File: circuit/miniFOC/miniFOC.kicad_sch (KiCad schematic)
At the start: 68 parts, among them J1 Conn_01x05, J2 Conn_01x06, J3 Conn_01x02, J4 Conn_01x01, J5 Conn_01x01, J6 Conn_01x01, Q1 AP30H50Q, Q2 AP30H50Q, Q3 AP30H50Q, Q4 AP30H50Q, Q5 AP30H50Q, Q6 AP30H50Q, U1 XC6206P332MR, U2 AT32F421C8, U3 LM321, U4 COS722MR, U5 EG2133, U6 JW5017S

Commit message: Completed PCB drawing of miniFOC sensor board
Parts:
- C26: footprint Capacitor_SMD:C_0603_1608Metric_Pad1.08x0.95mm_HandSolder -> Capacitor_SMD:C_0402_1005Metric
- C27, C28, C29: footprint Capacitor_SMD:C_0603_1608Metric_Pad1.08x0.95mm_HandSolder -> Capacitor_SMD:C_0603_1608Metric
- C3, C6: footprint Capacitor_SMD:C_1206_3216Metric_Pad1.33x1.80mm_HandSolder -> Capacitor_SMD:C_0603_1608Metric
- J2: footprint (none) -> Connector_JST:JST_GH_SM06B-GHS-TB_1x06-1MP_P1.25mm_Horizontal
- J3: footprint (none) -> Connector_Wire:SolderWire-0.1sqmm_1x02_P3.6mm_D0.4mm_OD1mm
- J4, J5, J6: footprint (none) -> Connector_PinHeader_2.54mm:PinHeader_1x01_P2.54mm_Vertical
- L1: footprint PowerLibrary:IND-SMD_L4.6-W4.2_SMMS0420 -> Inductor_SMD:L_Coilcraft_XxL4040
- R13, R15, R16: footprint Resistor_SMD:R_0603_1608Metric_Pad0.98x0.95mm_HandSolder -> Capacitor_SMD:C_0402_1005Metric
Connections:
- net TIM1_CH1: now also U5.3 (HIN3), U5.6 (~{LIN3}); no longer U5.1 (HIN1), U5.4 (~{LIN1})
- net TIM1_CH3: now also U5.1 (HIN1), U5.4 (~{LIN1}); no longer U5.3 (HIN3), U5.6 (~{LIN3})
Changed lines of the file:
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@@
   (title_block
     (title "miniFOC")
-    (date "2022-10-11")
+    (date "2022-10-21")
     (rev "1.2.1")
   )
@@
     (effects (font (size 1.27 1.27)) (justify right bottom))
   )
-  (label "TIM1_CH1" (at 153.67 55.88 0)
+  (label "TIM1_CH1" (at 153.67 60.96 0)
     (effects (font (size 1.27 1.27)) (justify left bottom))
   )
@@
     (effects (font (size 1.27 1.27)) (justify left bottom))
   )
-  (label "TIM1_CH3" (at 153.67 60.96 0)
+  (label "TIM1_CH3" (at 153.67 55.88 0)
     (effects (font (size 1.27 1.27)) (justify left bottom))
   )
@@
       (effects (font (size 1.27 1.27)) (justify left) hide)
     )
-    (property "Footprint" "" (id 2) (at 274.32 76.2 0)
+    (property "Footprint" "Connector_PinHeader_2.54mm:PinHeader_1x01_P2.54mm_Vertical" (id 2) (at 274.32 76.2 0)
       (effects (font (size 1.27 1.27)) hide)
     )
@@
       (effects (font (size 1.27 1.27)) (justify right) hide)
     )
-    (property "Footprint" "Capacitor_SMD:C_0603_1608Metric_Pad1.08x0.95mm_HandSolder" (id 2) (at 267.0048 151.13 0)
+    (property "Footprint" "Capacitor_SMD:C_0603_1608Metric" (id 2) (at 267.0048 151.13 0)
       (effects (font (size 1.27 1.27)) hide)
     )
@@
       (effects (font (size 1.27 1.27)) (justify right))
     )
-    (property "Footprint" "Capacitor_SMD:C_1206_3216Metric_Pad1.33x1.80mm_HandSolder" (id 2) (at 49.8348 177.8 0)
+    (property "Footprint" "Capacitor_SMD:C_0603_1608Metric" (id 2) (at 49.8348 177.8 0)
       (effects (font (size 1.27 1.27)) hide)
     )
@@
       (effects (font (size 1.27 1.27)) (justify right))
     )
-    (property "Footprint" "Capacitor_SMD:C_1206_3216Metric_Pad1.33x1.80mm_HandSolder" (id 2) (at 19.3548 177.8 0)
+    (property "Footprint" "Capacitor_SMD:C_0603_1608Metric" (id 2) (at 19.3548 177.8 0)
       (effects (font (size 1.27 1.27)) hide)
     )
@@
       (effects (font (size 1.27 1.27)) (justify right))
     )
-    (property "Footprint" "Capacitor_SMD:C_0603_1608Metric_Pad1.08x0.95mm_HandSolder" (id 2) (at 243.84 152.0952 0)
+    (property "Footprint" "Capacitor_SMD:C_0402_1005Metric" (id 2) (at 243.84 152.0952 0)
       (effects (font (size 1.27 1.27)) hide)
     )
@@
       (effects (font (size 1.27 1.27)) (justify right))
     )
-    (property "Footprint" "Resistor_SMD:R_0603_1608Metric_Pad0.98x0.95mm_HandSolder" (id 2) (at 222.758 143.51 90)
+    (property "Footprint" "Capacitor_SMD:C_0402_1005Metric" (id 2) (at 222.758 143.51 90)
       (effects (font (size 1.27 1.27)) hide)
     )
@@
       (effects (font (size 1.27 1.27)) (justify right) hide)
     )
-    (property "Footprint" "Capacitor_SMD:C_0603_1608Metric_Pad1.08x0.95mm_HandSolder" (id 2) (at 261.9248 163.83 0)
+    (property "Footprint" "Capacitor_SMD:C_0603_1608Metric" (id 2) (at 261.9248 163.83 0)
       (effects (font (size 1.27 1.27)) hide)
     )
@@
       (effects (font (size 1.27 1.27)) hide)
     )
-    (property "Footprint" "" (id 2) (at 180.34 157.48 0)
+    (property "Footprint" "Connector_Wire:SolderWire-0.1sqmm_1x02_P3.6mm_D0.4mm_OD1mm" (id 2) (at 180.34 157.48 0)
       (effects (font (size 1.27 1.27)) hide)
     )
@@
       (effects (font (size 1.27 1.27)) (justify left) hide)
     )
-    (property "Footprint" "" (id 2) (at 274.32 60.96 0)
+    (property "Footprint" "Connector_PinHeader_2.54mm:PinHeader_1x01_P2.54mm_Vertical" (id 2) (at 274.32 60.96 0)
       (effects (font (size 1.27 1.27)) hide)
     )
@@
       (effects (font (size 1.27 1.27)) (justify left) hide)
     )
-    (property "Footprint" "" (id 2) (at 134.62 40.64 0)
+    (property "Footprint" "Connector_JST:JST_GH_SM06B-GHS-TB_1x06-1MP_P1.25mm_Horizontal" (id 2) (at 134.62 40.64 0)
       (effects (font (size 1.27 1.27)) hide)
     )
@@
       (effects (font (size 1.27 1.27)) (justify left) hide)
     )
-    (property "Footprint" "" (id 2) (at 274.32 68.58 0)
+    (property "Footprint" "Connector_PinHeader_2.54mm:PinHeader_1x01_P2.54mm_Vertical" (id 2) (at 274.32 68.58 0)
       (effects (font (size 1.27 1.27)) hide)
     )
@@
       (effects (font (size 1.27 1.27)) (justify right))
     )
-    (property "Footprint" "Capacitor_SMD:C_0603_1608Metric_Pad1.08x0.95mm_HandSolder" (id 2) (at 273.3548 151.13 0)
+    (property "Footprint" "Capacitor_SMD:C_0603_1608Metric" (id 2) (at 273.3548 151.13 0)
       (effects (font (size 1.27 1.27)) hide)
     )
@@
       (effects (font (size 1.27 1.27)) (justify right))
     )
-    (property "Footprint" "Resistor_SMD:R_0603_1608Metric_Pad0.98x0.95mm_HandSolder" (id 2) (at 245.618 168.91 90)
+    (property "Footprint" "Capacitor_SMD:C_0402_1005Metric" (id 2) (at 245.618 168.91 90)
       (effects (font (size 1.27 1.27)) hide)
     )
@@
     (property "Reference" "L1" (id 0) (at 257.81 148.59 90))
     (property "Value" "4.7uH" (id 1) (at 257.81 151.13 90))
-    (property "Footprint" "PowerLibrary:IND-SMD_L4.6-W4.2_SMMS0420" (id 2) (at 257.81 153.67 0)
+    (property "Footprint" "Inductor_SMD:L_Coilcraft_XxL4040" (id 2) (at 257.81 153.67 0)
       (effects (font (size 1.27 1.27)) hide)
     )
@@
     (property "Reference" "R16" (id 0) (at 253.365 162.56 90))
     (property "Value" "16kR" (id 1) (at 253.365 164.465 90))
-    (property "Footprint" "Resistor_SMD:R_0603_1608Metric_Pad0.98x0.95mm_HandSolder" (id 2) (at 253.365 158.242 90)
+    (property "Footprint" "Capacitor_SMD:C_0402_1005Metric" (id 2) (at 253.365 158.242 90)
       (effects (font (size 1.27 1.27)) hide)
     )
@@
     )
     (path "/57180d6e-6a91-467d-a82b-02bb6d697214"
-      (reference "C3") (unit 1) (value "10uF") (footprint "Capacitor_SMD:C_1206_3216Metric_Pad1.33x1.80mm_HandSolder")
+      (reference "C3") (unit 1) (value "10uF") (footprint "Capacitor_SMD:C_0603_1608Metric")
     )
     (path "/ebd293f8-a987-417b-a4c4-abe8a2adfd97"
@@
     )
     (path "/1af18610-1415-484c-99c1-d2085ea98a87"
-      (reference "C6") (unit 1) (value "10uF") (footprint "Capacitor_SMD:C_1206_3216Metric_Pad1.33x1.80mm_HandSolder")
+      (reference "C6") (unit 1) (value "10uF") (footprint "Capacitor_SMD:C_0603_1608Metric")
     )
     (path "/5de879fb-dac5-44c4-8df6-5853ed3f2d44"
@@
     )
     (path "/6d0a8729-3a54-430f-8b0f-be4deb3d1c1a"
-      (reference "C26") (unit 1) (value "100nF") (footprint "Capacitor_SMD:C_0603_1608Metric_Pad1.08x0.95mm_HandSolder")
+      (reference "C26") (unit 1) (value "100nF") (footprint "Capacitor_SMD:C_0402_1005Metric")
     )
     (path "/8836bf46-cefc-4f20-9228-b7aa312d1021"
-      (reference "C27") (unit 1) (value "22uF") (footprint "Capacitor_SMD:C_0603_1608Metric_Pad1.08x0.95mm_HandSolder")
+      (reference "C27") (unit 1) (value "22uF") (footprint "Capacitor_SMD:C_0603_1608Metric")
     )
     (path "/15e769c6-5c6f-4f78-96ac-500286d22897"
-      (reference "C28") (unit 1) (value "22uF") (footprint "Capacitor_SMD:C_0603_1608Metric_Pad1.08x0.95mm_HandSolder")
+      (reference "C28") (unit 1) (value "22uF") (footprint "Capacitor_SMD:C_0603_1608Metric")
     )
     (path "/cc13aa9b-0a71-47d7-a701-77ff3ce296df"
-      (reference "C29") (unit 1) (value "22uF") (footprint "Capacitor_SMD:C_0603_1608Metric_Pad1.08x0.95mm_HandSolder")
+      (reference "C29") (unit 1) (value "22uF") (footprint "Capacitor_SMD:C_0603_1608Metric")
     )
     (path "/b588f9f0-2e7b-4276-bdc3-13441b671919"
@@
     )
     (path "/b8cd981c-8223-4dd3-9974-b8b75ac48f6b"
-      (reference "J2") (unit 1) (value "Conn_01x06") (footprint "")
+      (reference "J2") (unit 1) (value "Conn_01x06") (footprint "Connector_JST:JST_GH_SM06B-GHS-TB_1x06-1MP_P1.25mm_Horizontal")
     )
     (path "/ac186fed-923a-47cd-8a16-7ed09e712c31"
-      (reference "J3") (unit 1) (value "Conn_01x02") (footprint "")
+      (reference "J3") (unit 1) (value "Conn_01x02") (footprint "Connector_Wire:SolderWire-0.1sqmm_1x02_P3.6mm_D0.4mm_OD1mm")
     )
     (path "/b79a7217-3e47-495b-8bfb-0863fe190bae"
-      (reference "J4") (unit 1) (value "Conn_01x01") (footprint "")
+      (reference "J4") (unit 1) (value "Conn_01x01") (footprint "Connector_PinHeader_2.54mm:PinHeader_1x01_P2.54mm_Vertical")
     )
     (path "/c2d45456-c1f1-4f70-b49f-799529a01b00"
-      (reference "J5") (unit 1) (value "Conn_01x01") (footprint "")
+      (reference "J5") (unit 1) (value "Conn_01x01") (footprint "Connector_PinHeader_2.54mm:PinHeader_1x01_P2.54mm_Vertical")
     )
     (path "/031104e4-2843-42a8-88a2-40956a4b8fbd"
-      (reference "J6") (unit 1) (value "Conn_01x01") (footprint "")
+      (reference "J6") (unit 1) (value "Conn_01x01") (footprint "Connector_PinHeader_2.54mm:PinHeader_1x01_P2.54mm_Vertical")
     )
     (path "/f600ef09-3064-4eca-945e-e4a8c4ccc8ae"
-      (reference "L1") (unit 1) (value "4.7uH") (footprint "PowerLibrary:IND-SMD_L4.6-W4.2_SMMS0420")
+      (reference "L1") (unit 1) (value "4.7uH") (footprint "Inductor_SMD:L_Coilcraft_XxL4040")
     )
     (path "/26885aef-6433-45fe-8034-e15ff2fb5127"
@@
     )
     (path "/821d8552-41c4-43a7-974e-33c697d9f8f0"
-      (reference "R13") (unit 1) (value "100kR") (footprint "Resistor_SMD:R_0603_1608Metric_Pad0.98x0.95mm_HandSolder")
+      (reference "R13") (unit 1) (value "100kR") (footprint "Capacitor_SMD:C_0402_1005Metric")
     )
     (path "/2a16502b-c1b0-457f-9456-252e2d31aed9"
@@
     )
     (path "/ce128697-0de6-45fe-83ae-9161148ee65f"
-      (reference "R15") (unit 1) (value "3kR") (footprint "Resistor_SMD:R_0603_1608Metric_Pad0.98x0.95mm_HandSolder")
+      (reference "R15") (unit 1) (value "3kR") (footprint "Capacitor_SMD:C_0402_1005Metric")
     )
     (path "/ff6c7184-0e54-47b1-9869-6205f7198afa"
-      (reference "R16") (unit 1) (value "16kR") (footprint "Resistor_SMD:R_0603_1608Metric_Pad0.98x0.95mm_HandSolder")
+      (reference "R16") (unit 1) (value "16kR") (footprint "Capacitor_SMD:C_0402_1005Metric")
     )
     (path "/fb155bda-005a-4de1-879d-15ff861b4a76"

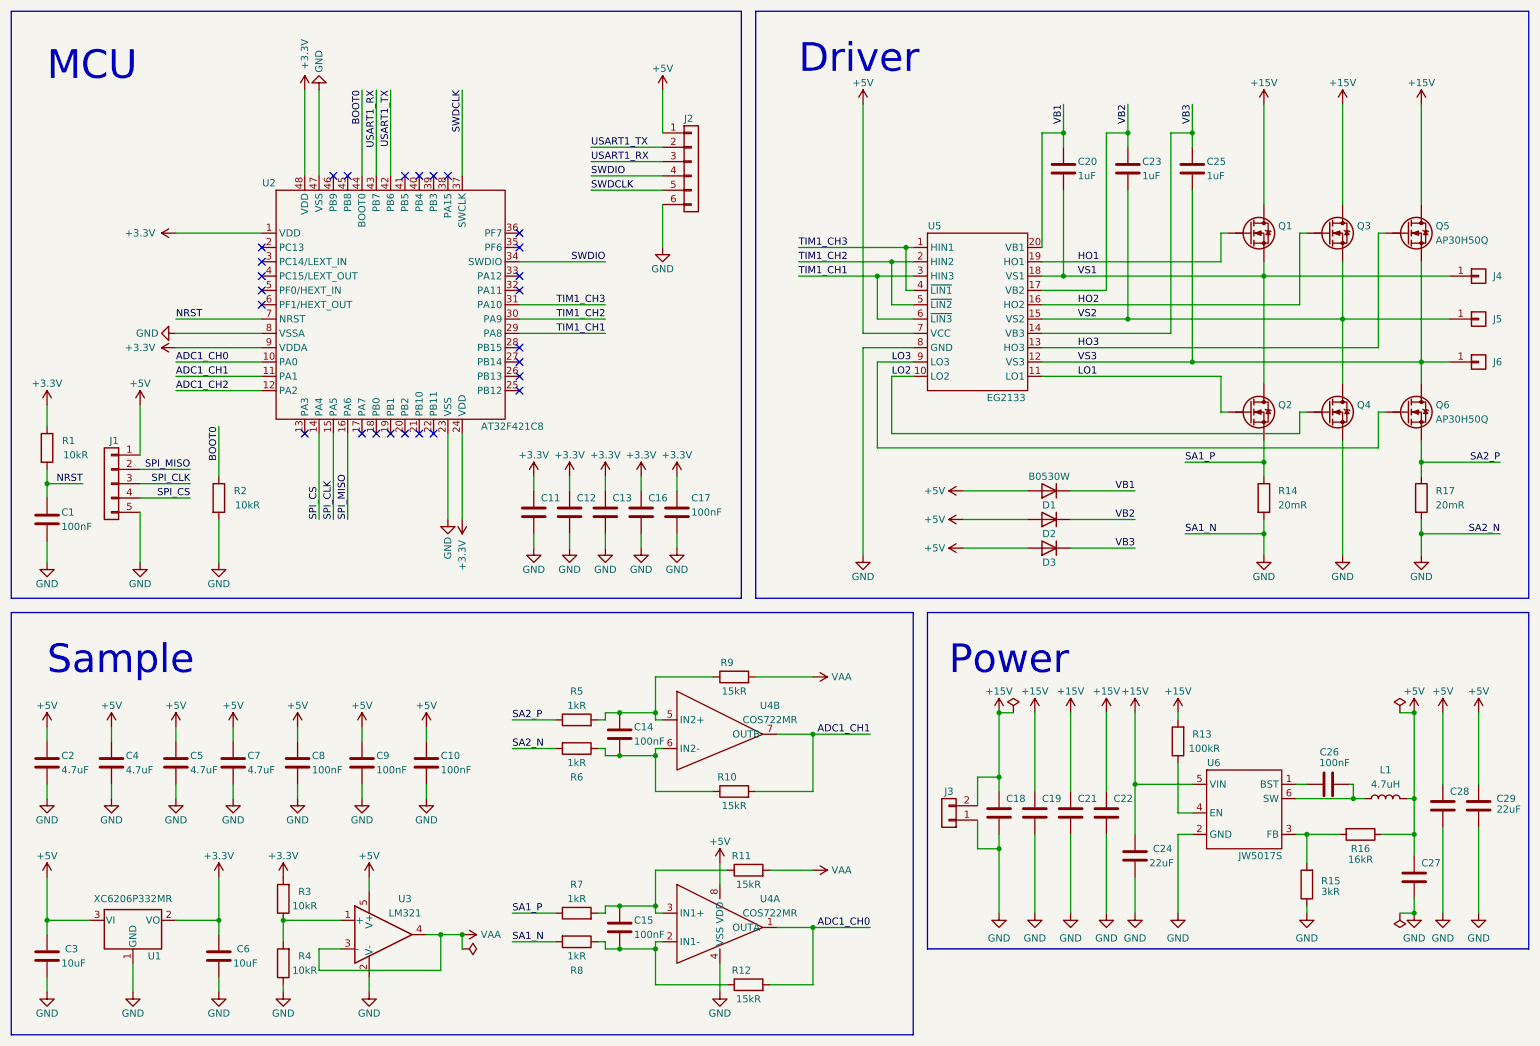
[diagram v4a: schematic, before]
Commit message: Replace the power stage with a one-piece half bridge with integrated gate drive
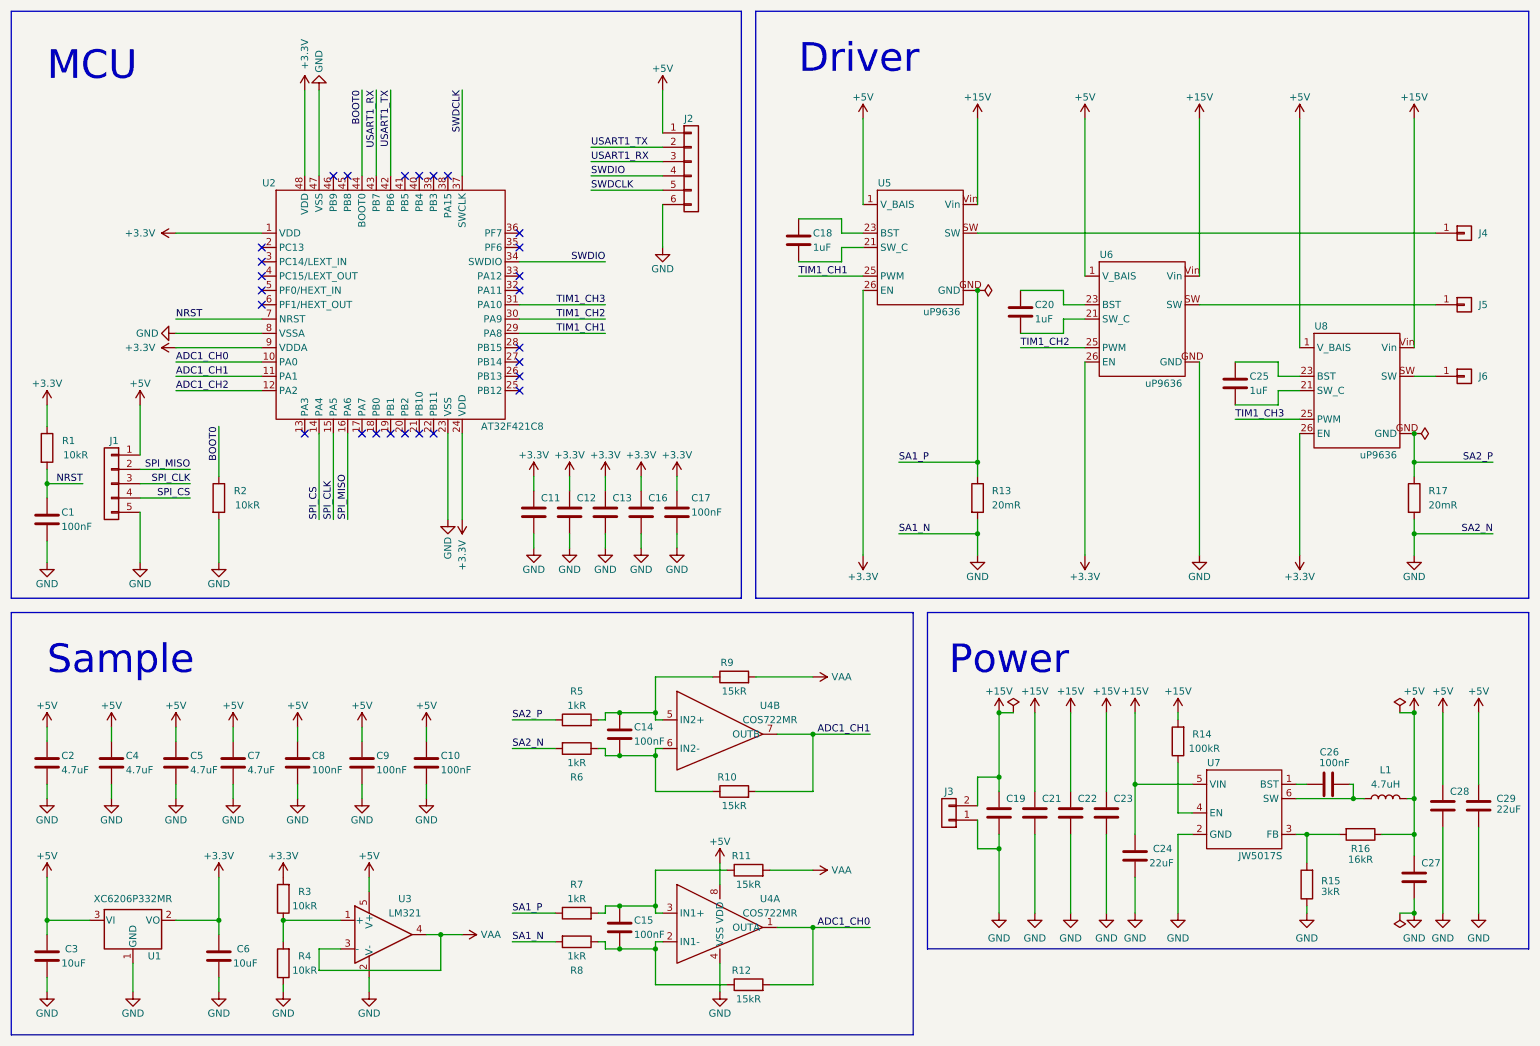
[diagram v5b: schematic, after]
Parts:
- removed C23: 1uF, Capacitor_SMD:C_0402_1005Metric, symbol Device:C
- removed D1, D2, D3: B0530W, Diode_SMD:D_SOD-123, symbol Diode:1N4148W
- removed Q1, Q2, Q3, Q4, Q5, Q6: AP30H50Q, Package_SON:VSON-8_3.3x3.3mm_P0.65mm_NexFET, symbol Library:AP30H50Q
- removed U5: EG2133, Package_SO:TSSOP-20_4.4x6.5mm_P0.65mm, symbol Library:EG2133
- added C20: 1uF, Capacitor_SMD:C_0402_1005Metric, symbol Device:C
- added U5, U6, U8: uP9636, Library:QFN-26_4040_IPS, symbol Library:uP9636
- renumbered C20 to C18, C18 to C19, C19 to C21, C21 to C22, C22 to C23, R14 to R13, R13 to R14, U6 to U7
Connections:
- net +15V: now also U5.Vin, U6.Vin, U8.Vin
- net +3.3V: now also U5.26 (EN), U6.26 (EN), U8.26 (EN)
- net +5V: now also U5.1 (V_BAIS), U6.1 (V_BAIS), U8.1 (V_BAIS)
- net GND: now also U6.GND
- net SA1_P: now also U5.GND
- net SA2_P: now also U8.GND
- net TIM1_CH1: now also U5.25 (PWM)
- net TIM1_CH2: now also U6.25 (PWM)
- net TIM1_CH3: now also U8.25 (PWM)
- net VB1: no longer names the net of C18.1
- net VB1: now also U5.23 (BST)
- net VB3: no longer names the net of C25.1
- net VB3: now also U8.23 (BST)
- net VS1: no longer names the net of C18.2
- net VS1: now also U5.21 (SW_C); no longer J4.1 (Pin_1)
- net VS2: no longer names the net of J5.1 (Pin_1)
- net VS2: now also U6.SW
- net VS3: no longer names the net of J6.1 (Pin_1)
- net VS3: now also U8.SW; no longer C25.2
- new net: C25.2, U8.21 (SW_C)
- new net: J4.1 (Pin_1), U5.SW
- new net: C20.2, U6.21 (SW_C)
- new net: C20.1, U6.23 (BST)
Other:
- moved on the sheet: C18, J4, J5, J6, R13, R17
